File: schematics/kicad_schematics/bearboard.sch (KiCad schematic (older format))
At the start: 1 part

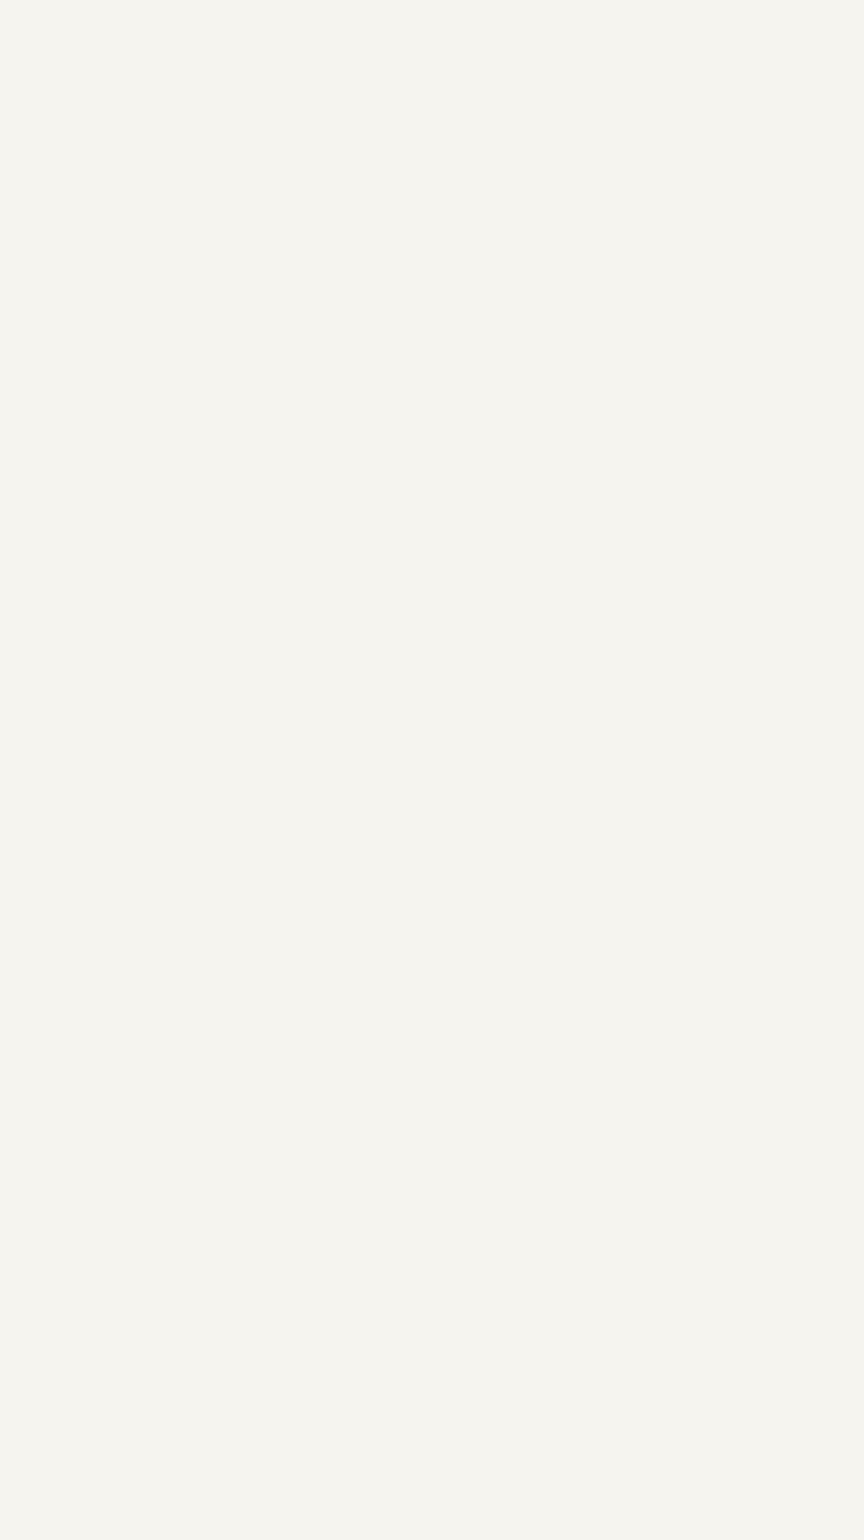
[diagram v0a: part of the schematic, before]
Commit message: Added schematic files
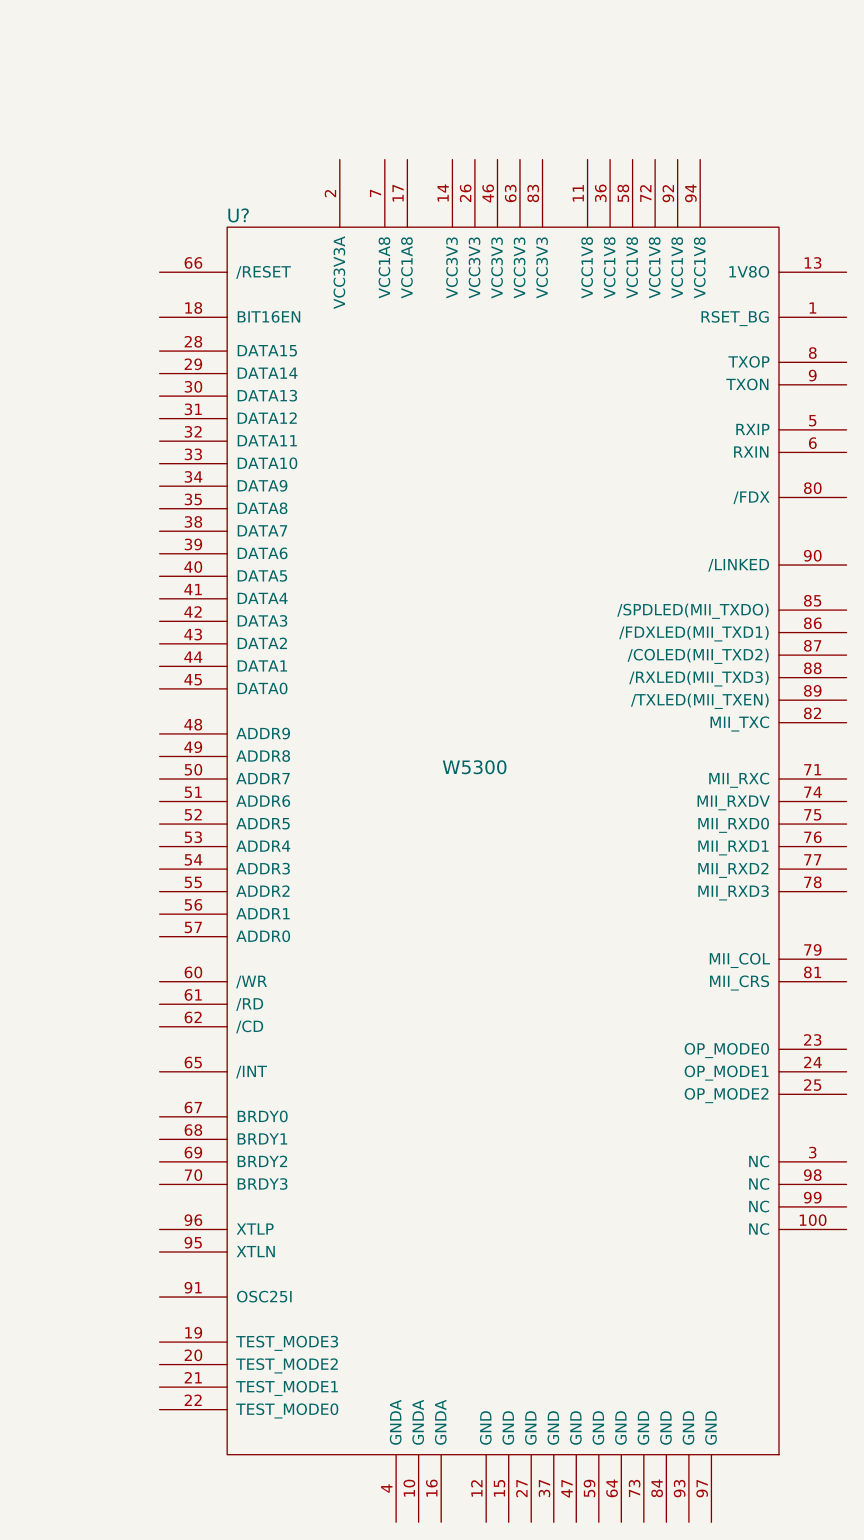
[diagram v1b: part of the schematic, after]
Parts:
- added U?: W5300, symbol W5300
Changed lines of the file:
@@
-EESchema Schematic File Version 2  date Sat 06 Feb 2010 12:13:34 AM EST
+EESchema Schematic File Version 2  date Sat 06 Feb 2010 01:15:14 AM EST
 LIBS:power
 LIBS:device
@@
 EELAYER 24  0
 EELAYER END
-$Descr A4 11700 8267
+$Descr C 22000 17000
 Sheet 1 1
-Title ""
+Title "BearBoard STM32F103"
 Date "6 feb 2010"
-Rev ""
-Comp ""
-Comment1 ""
+Rev "0"
+Comp "University of Maine"
+Comment1 "Author: Jason Withee"
 Comment2 ""
 Comment3 ""
@@
 $EndDescr
 $Comp
+L W5300 U?
+U 1 1 4B6D08E6
+P 14100 7050
+F 0 "U?" H 12950 9450 60  0000 C CNN
+F 1 "W5300" H 14000 7000 60  0000 C CNN
+	1    14100 7050
+	1    0    0    -1
+$EndComp
+$Comp
 L STM32F103 U?

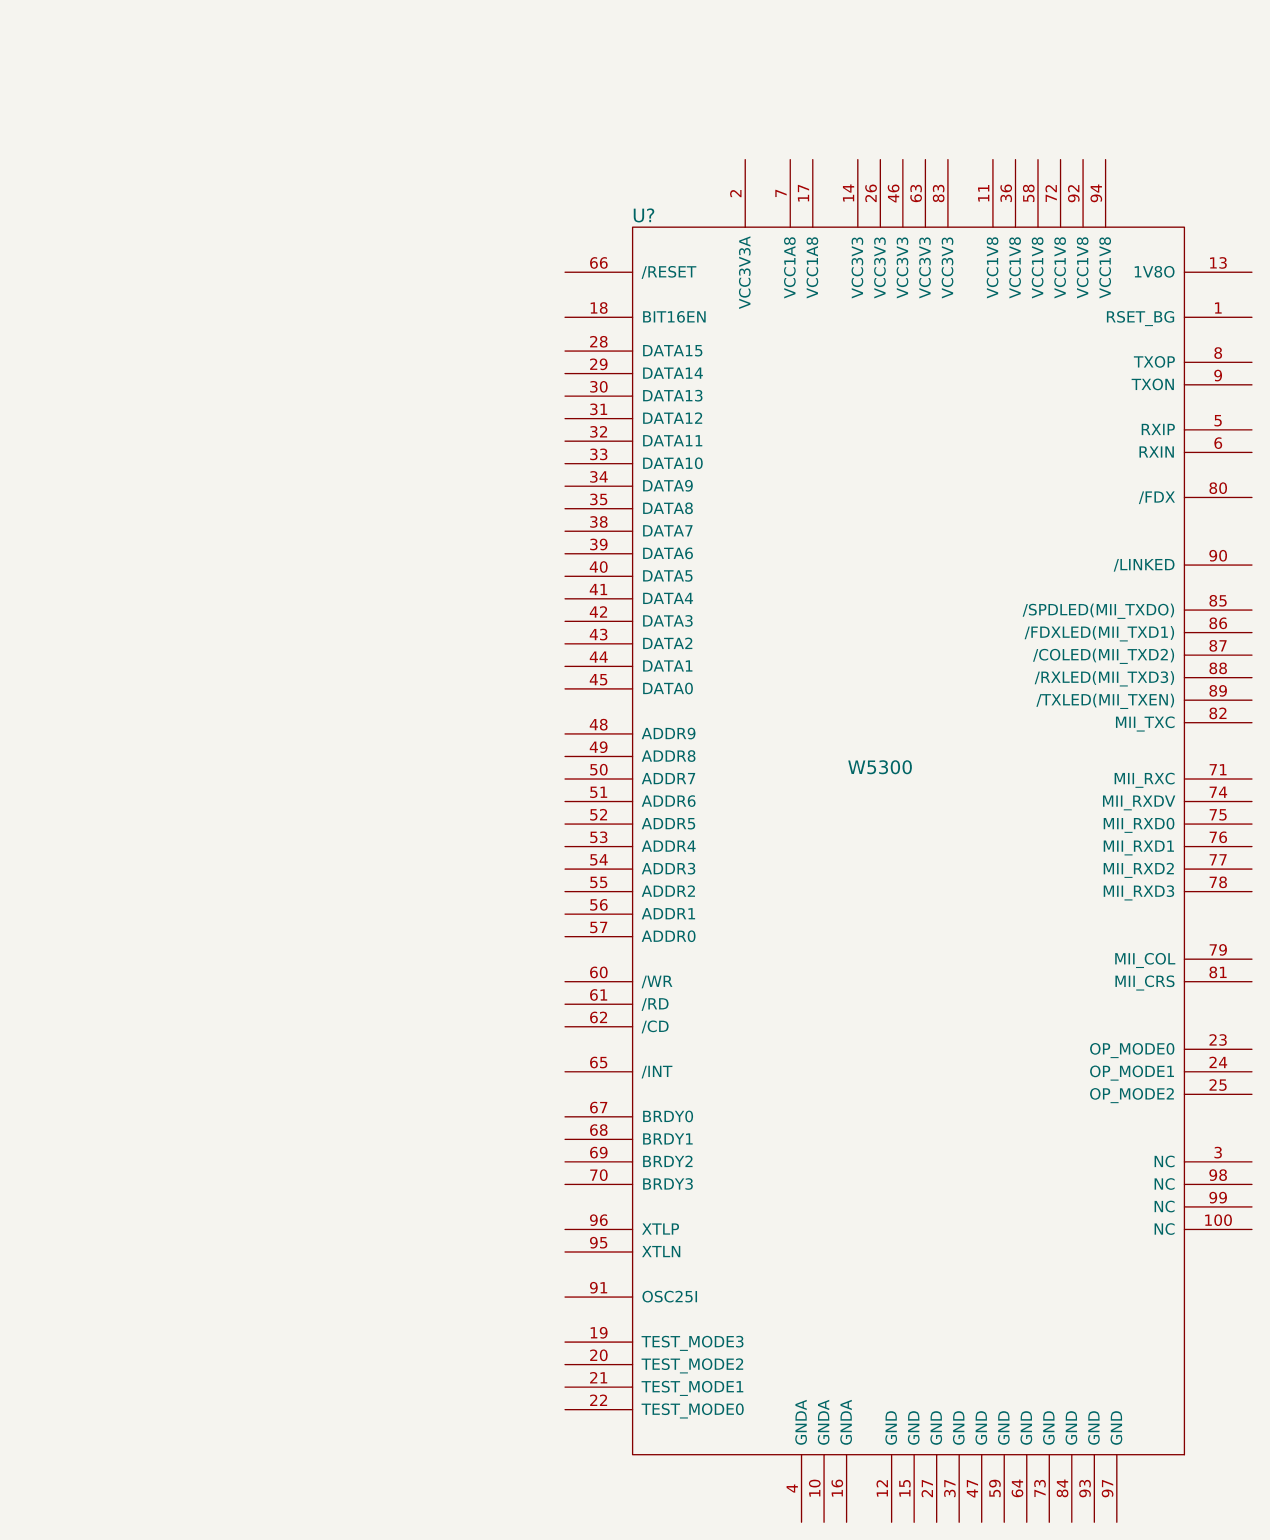
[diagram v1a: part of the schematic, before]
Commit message: Added schematic Wiznet chips and subsheets
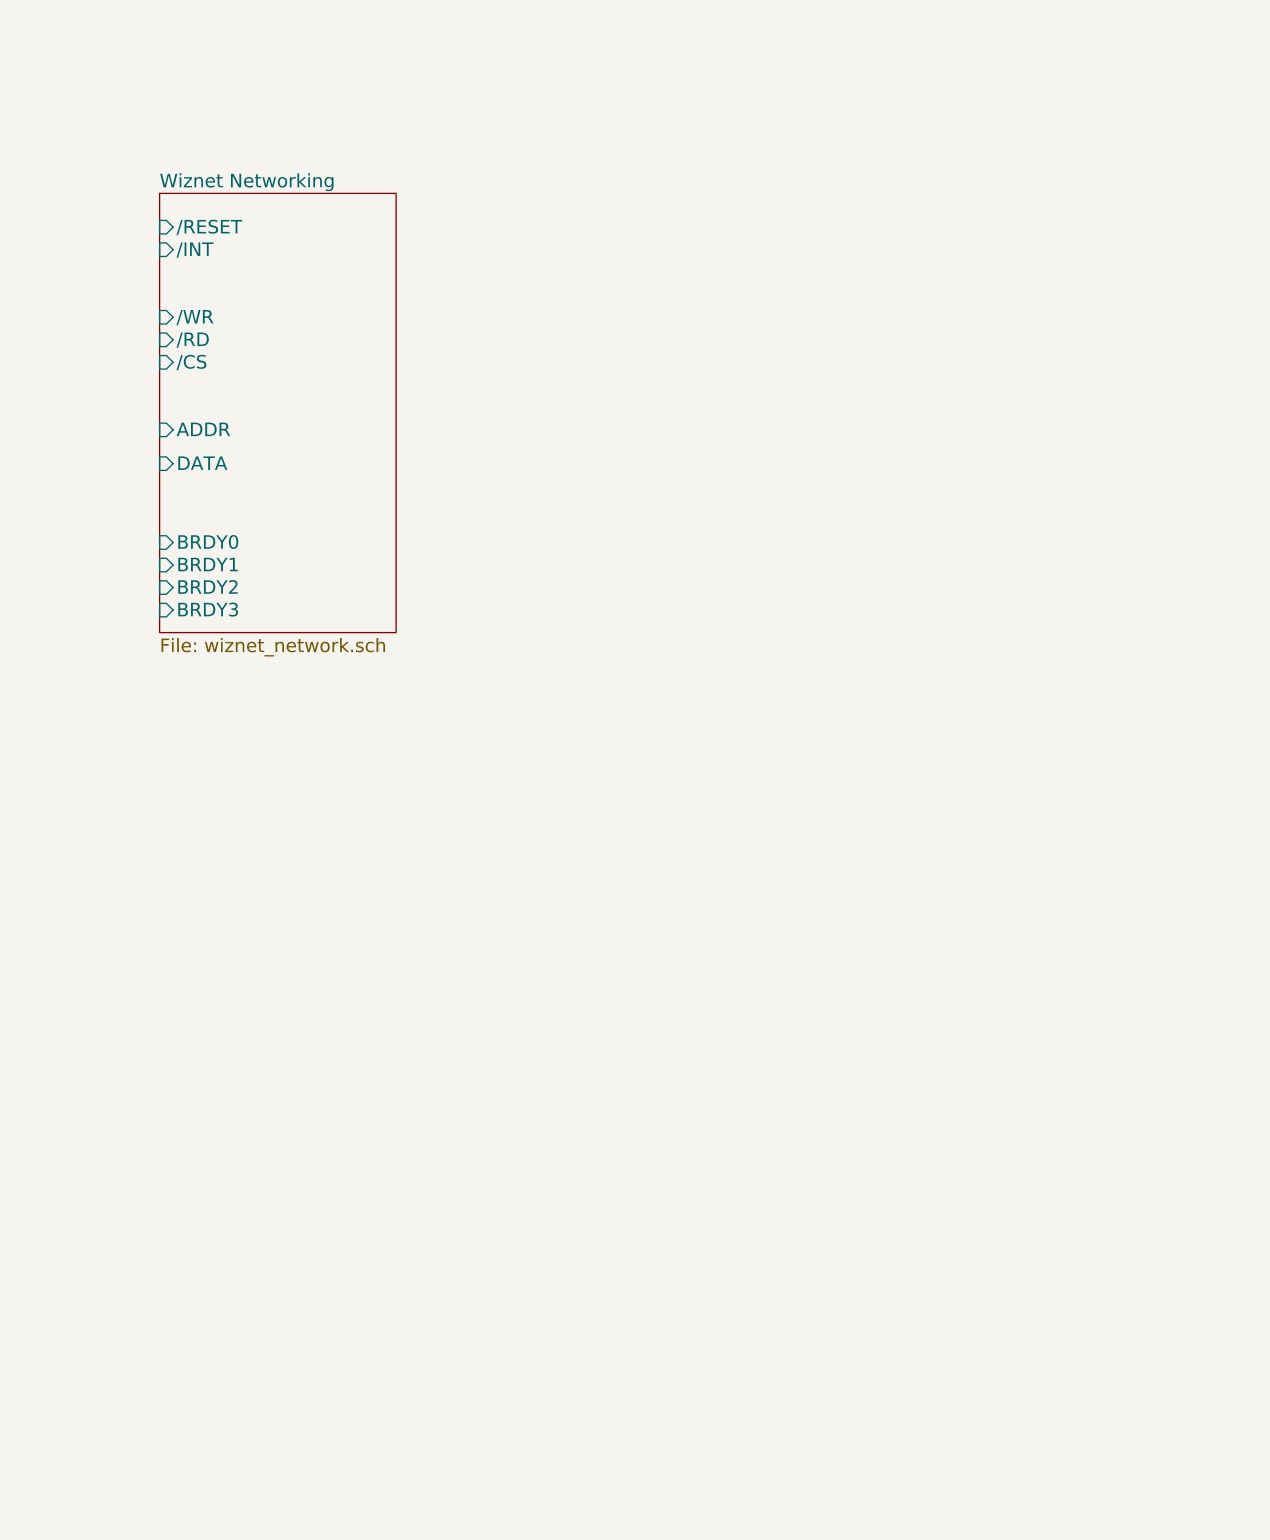
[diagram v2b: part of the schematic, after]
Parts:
- removed U?: W5300, symbol W5300
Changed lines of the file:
@@
-EESchema Schematic File Version 2  date Sat 06 Feb 2010 01:15:14 AM EST
+EESchema Schematic File Version 2  date Sat 06 Feb 2010 02:58:11 PM EST
+LIBS:bearboard-cache
 LIBS:power
 LIBS:device
@@
 LIBS:stm32
 LIBS:wiznet
-LIBS:bearboard-cache
+LIBS:dips-s
 EELAYER 24  0
 EELAYER END
 $Descr C 22000 17000
-Sheet 1 1
+Sheet 1 2
 Title "BearBoard STM32F103"
 Date "6 feb 2010"
@@
 Comment4 ""
 $EndDescr
-$Comp
-L W5300 U?
-U 1 1 4B6D08E6
-P 14100 7050
-F 0 "U?" H 12950 9450 60  0000 C CNN
-F 1 "W5300" H 14000 7000 60  0000 C CNN
-	1    14100 7050
-	1    0    0    -1
-$EndComp
+$Sheet
+S 10800 4550 1050 1950
+U 4B6DAA26
+F0 "Wiznet Networking" 60
+F1 "wiznet_network.sch" 60
+F2 "/RESET" I L 10800 4700 60
+F3 "BRDY3" I L 10800 6400 60
+F4 "BRDY2" I L 10800 6300 60
+F5 "BRDY1" I L 10800 6200 60
+F6 "BRDY0" I L 10800 6100 60
+F7 "/INT" I L 10800 4800 60
+F8 "/RD" I L 10800 5200 60
+F9 "/CS" I L 10800 5300 60
+F10 "/WR" I L 10800 5100 60
+F11 "ADDR" I L 10800 5600 60
+F12 "DATA" I L 10800 5750 60
+$EndSheet
 $Comp
 L STM32F103 U?

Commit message: added some eval stuff
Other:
- moved on the sheet: U?
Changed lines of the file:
@@
-EESchema Schematic File Version 2  date Sat 06 Feb 2010 02:58:11 PM EST
-LIBS:bearboard-cache
+EESchema Schematic File Version 2  date Thu 18 Feb 2010 09:31:45 PM EST
 LIBS:power
 LIBS:device
@@
 LIBS:wiznet
 LIBS:dips-s
+LIBS:bearboard-cache
 EELAYER 24  0
 EELAYER END
@@
 Sheet 1 2
 Title "BearBoard STM32F103"
-Date "6 feb 2010"
+Date "19 feb 2010"
 Rev "0"
 Comp "University of Maine"
@@
 L STM32F103 U?
 U 1 1 4B6CFA5E
-P 5000 450
-F 0 "U?" H 2450 650 60  0000 C CNN
-F 1 "STM32F103" H 2750 -7250 60  0000 C CNN
-	1    5000 450
+P 5150 3600
+F 0 "U?" H 2600 3800 60  0000 C CNN
+F 1 "STM32F103" H 2900 -4100 60  0000 C CNN
+	1    5150 3600
 	1    0    0    -1
 $EndComp

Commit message: modified schematic
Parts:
- added R? (x5): 47K, symbol R
- added U?: SD_CARD, symbol SD_CARD
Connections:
- net labels added: 3V3, ADDR0, ADDR1, ADDR10, ADDR11, ADDR12, ADDR13, ADDR14, ADDR15, ADDR2, ADDR3, ADDR4, ADDR5, ADDR6, ADDR7, ADDR8, ADDR9, D0, D1, D10, D11, D12, D13, D14, D15, D2, D3, D4, D5, D6, D7, D8, D9, GND, SD_CD, SD_CLK, SD_CMD, SD_DAT0, SD_DAT1, SD_DAT2, SD_DAT3, SD_WD
- wire segments 0 -> 60

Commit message: added more to the schematic
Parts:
- removed U?: SD_CARD, symbol SD_CARD
- added C? (x2): C, symbol C
- added R?: R, symbol R
- added X?: CRYSTAL, symbol CRYSTAL
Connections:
- net labels added: OSC_IN, OSC_OUT, USB_DM, USB_DP, USB_Disconnect
- wire segments 60 -> 75
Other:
- moved on the sheet: U?

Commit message: added more to the schematic
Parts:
- added C? (x2): 10pF, symbol C
- added R?: 10K, symbol R
- added SW?: SWITCH_INV, symbol SWITCH_INV
- added X?: 32.768KHz, symbol CRYSTAL
- C? (x2): value C -> 20pF
- R?: value R -> 390
- X?: value CRYSTAL -> 8-16MHz
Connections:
- net labels added: OSC32_IN, OSC32_OUT
- wire segments 75 -> 90
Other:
- moved on the sheet: C?, R?, X?
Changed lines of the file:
@@
-EESchema Schematic File Version 2  date Fri 19 Feb 2010 09:12:18 AM EST
+EESchema Schematic File Version 2  date Fri 19 Feb 2010 09:38:21 AM EST
 LIBS:power
 LIBS:device
@@
 Comment4 ""
 $EndDescr
-Text Label 3650 10750 1    60   ~ 0
-OSC_OUT
-Text Label 2750 10800 1    60   ~ 0
-OSC_IN
-Connection ~ 3650 11600
-Wire Wire Line
-	3650 11400 3650 11700
-Wire Wire Line
-	2750 11600 2900 11600
-Wire Wire Line
-	3650 12100 3650 12200
-Wire Wire Line
-	3650 12200 2750 12200
-Wire Wire Line
-	2750 12200 2750 12100
+Wire Wire Line
+	2500 6800 2350 6800
+Wire Wire Line
+	2850 6850 2850 6850
+Connection ~ 3100 12800
+Wire Wire Line
+	3100 12900 3100 11700
+Wire Wire Line
+	4000 12800 3850 12800
+Connection ~ 3550 13400
+Wire Wire Line
+	3550 13450 3550 13400
+Wire Wire Line
+	3100 13300 3100 13400
+Wire Wire Line
+	3100 13400 4000 13400
+Wire Wire Line
+	4000 13400 4000 13300
+Wire Wire Line
+	3250 12800 3100 12800
+Connection ~ 4000 12800
+Wire Wire Line
+	3400 7200 4350 7200
+Wire Wire Line
+	3400 7100 4350 7100
+Connection ~ 2350 12850
+Wire Wire Line
+	2350 12950 2350 12650
+Wire Wire Line
+	1450 12850 1600 12850
+Wire Wire Line
+	2350 13350 2350 13450
+Wire Wire Line
+	2350 13450 1450 13450
+Wire Wire Line
+	1450 13450 1450 13350
 Wire Wire Line
 	9750 12100 8850 12100
@@
 	16700 10550 18800 10550
 Wire Wire Line
-	16700 10250 18800 10250
-Wire Wire Line
-	16700 9200 18800 9200
+	18800 10250 16700 10250
+Wire Wire Line
+	18800 9200 16700 9200
 Wire Wire Line
 	16700 9800 18800 9800
@@
 	18700 9650 18800 9650
 Wire Wire Line
-	16700 9350 18800 9350
-Wire Wire Line
-	16700 10100 18800 10100
-Wire Wire Line
-	16700 10400 18800 10400
+	18800 9350 16700 9350
+Wire Wire Line
+	18800 10100 16700 10100
+Wire Wire Line
+	18800 10400 16700 10400
 Wire Wire Line
 	16700 10700 18800 10700
@@
 	4350 5000 3400 5000
 Wire Wire Line
-	3200 12250 3200 12200
-Connection ~ 3200 12200
-Wire Wire Line
-	3650 11600 3500 11600
-Wire Wire Line
-	2750 10500 2750 11700
-Connection ~ 2750 11600
-Wire Wire Line
-	3650 10500 3650 10900
+	1900 13500 1900 13450
+Connection ~ 1900 13450
+Wire Wire Line
+	2200 12850 2350 12850
+Wire Wire Line
+	1450 12950 1450 11750
+Connection ~ 1450 12850
+Wire Wire Line
+	2350 11750 2350 12150
+Wire Wire Line
+	4000 11700 4000 12900
+Wire Wire Line
+	3400 6600 4350 6600
+Wire Wire Line
+	3400 6700 4350 6700
+Wire Wire Line
+	4350 6800 3000 6800
+$Comp
+L R R?
+U 1 1 4B7EA186
+P 2750 6800
+F 0 "R?" V 2830 6800 50  0000 C CNN
+F 1 "10K" V 2750 6800 50  0000 C CNN
+	1    2750 6800
+	0    1    1    0
+$EndComp
+$Comp
+L SWITCH_INV SW?
+U 1 1 4B7EA152
+P 1850 6800
+F 0 "SW?" H 1650 6950 50  0000 C CNN
+F 1 "SWITCH_INV" H 1700 6650 50  0000 C CNN
+	1    1850 6800
+	-1   0    0    1
+$EndComp
+Text Label 3400 6600 0    60   ~ 0
+OSC32_IN
+Text Label 3400 6700 0    60   ~ 0
+OSC32_OUT
+$Comp
+L CRYSTAL X?
+U 1 1 4B7EA0BC
+P 3550 12800
+F 0 "X?" H 3550 12950 60  0000 C CNN
+F 1 "32.768KHz" H 3550 12650 60  0000 C CNN
+	1    3550 12800
+	1    0    0    -1
+$EndComp
+$Comp
+L C C?
+U 1 1 4B7EA0BB
+P 4000 13100
+F 0 "C?" H 4050 13200 50  0000 L CNN
+F 1 "10pF" H 4050 13000 50  0000 L CNN
+	1    4000 13100
+	1    0    0    -1
+$EndComp
+$Comp
+L C C?
+U 1 1 4B7EA0BA
+P 3100 13100
+F 0 "C?" H 3150 13200 50  0000 L CNN
+F 1 "10pF" H 3150 13000 50  0000 L CNN
+	1    3100 13100
+	1    0    0    -1
+$EndComp
+$Comp
+L GND #PWR?
+U 1 1 4B7EA0B9
+P 3550 13450
+F 0 "#PWR?" H 3550 13450 30  0001 C CNN
+F 1 "GND" H 3550 13380 30  0001 C CNN
+	1    3550 13450
+	1    0    0    -1
+$EndComp
+Text Label 3100 12200 1    60   ~ 0
+OSC32_IN
+Text Label 4000 12200 1    60   ~ 0
+OSC32_OUT
+Text Label 3400 7200 0    60   ~ 0
+OSC_OUT
+Text Label 3400 7100 0    60   ~ 0
+OSC_IN
+Text Label 2350 12000 1    60   ~ 0
+OSC_OUT
+Text Label 1450 12050 1    60   ~ 0
+OSC_IN
 $Comp
 L R R?
 U 1 1 4B7E9BF1
-P 3650 11150
-F 0 "R?" V 3730 11150 50  0000 C CNN
-F 1 "R" V 3650 11150 50  0000 C CNN
-	1    3650 11150
+P 2350 12400
+F 0 "R?" V 2430 12400 50  0000 C CNN
+F 1 "390" V 2350 12400 50  0000 C CNN
+	1    2350 12400
 	1    0    0    -1
 $EndComp
@@
 L GND #PWR?
 U 1 1 4B7E9BE8
-P 3200 12250
-F 0 "#PWR?" H 3200 12250 30  0001 C CNN
-F 1 "GND" H 3200 12180 30  0001 C CNN
-	1    3200 12250
+P 1900 13500
+F 0 "#PWR?" H 1900 13500 30  0001 C CNN
+F 1 "GND" H 1900 13430 30  0001 C CNN
+	1    1900 13500
 	1    0    0    -1
 $EndComp
@@
 L C C?
 U 1 1 4B7E9BCF
-P 2750 11900
-F 0 "C?" H 2800 12000 50  0000 L CNN
-F 1 "C" H 2800 11800 50  0000 L CNN
-	1    2750 11900
+P 1450 13150
+F 0 "C?" H 1500 13250 50  0000 L CNN
+F 1 "20pF" H 1500 13050 50  0000 L CNN
+	1    1450 13150
 	1    0    0    -1
 $EndComp
@@
 L C C?
 U 1 1 4B7E9BCB
-P 3650 11900
-F 0 "C?" H 3700 12000 50  0000 L CNN
-F 1 "C" H 3700 11800 50  0000 L CNN
-	1    3650 11900
+P 2350 13150
+F 0 "C?" H 2400 13250 50  0000 L CNN
+F 1 "20pF" H 2400 13050 50  0000 L CNN
+	1    2350 13150
 	1    0    0    -1
 $EndComp
@@
 L CRYSTAL X?
 U 1 1 4B7E9BC1
-P 3200 11600
-F 0 "X?" H 3200 11750 60  0000 C CNN
-F 1 "CRYSTAL" H 3200 11450 60  0000 C CNN
-	1    3200 11600
-	1    0    0    -1
-$EndComp
+P 1900 12850
+F 0 "X?" H 1900 13000 60  0000 C CNN
+F 1 "8-16MHz" H 1900 12700 60  0000 C CNN
+	1    1900 12850
+	1    0    0    -1
+$EndComp
